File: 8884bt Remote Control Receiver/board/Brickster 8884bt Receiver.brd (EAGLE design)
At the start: 28.8 x 28.8 mm, 22 parts, among them IC2 IC_RT9164A, J1 AVR_SPI_PRG_6NS, J2 CON_PF, J3 CON_PF, J4 CON_PF, U1 IC_ATTINY_X4A, U2 IC_TB6612FNG

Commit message: Add second mounting tab
provides more stability
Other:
- outline, holes or cut-outs redrawn
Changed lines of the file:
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@@
 <wire x1="0" y1="19.9644" x2="0.8128" y2="20.7772" width="0" layer="20" curve="-90"/>
 <wire x1="28.7528" y1="19.9644" x2="27.94" y2="20.7772" width="0" layer="20" curve="90"/>
-<wire x1="10.3886" y1="21.1836" x2="10.3886" y2="27.94" width="0" layer="20"/>
-<wire x1="9.5758" y1="28.7528" x2="7.2644" y2="28.7528" width="0" layer="20"/>
-<wire x1="5.588" y1="28.7528" x2="3.2258" y2="28.7528" width="0" layer="20"/>
-<wire x1="2.413" y1="27.94" x2="2.413" y2="21.1836" width="0" layer="20"/>
-<wire x1="4.064" y1="26.3398" x2="8.7376" y2="26.3398" width="0" layer="20" curve="180"/>
-<wire x1="4.064" y1="26.3398" x2="5.588" y2="28.5496" width="0" layer="20" curve="-69.007147"/>
-<wire x1="8.7376" y1="26.3398" x2="7.2644" y2="28.5496" width="0" layer="20" curve="69.007147"/>
-<wire x1="2.0066" y1="20.7772" x2="2.413" y2="21.1836" width="0" layer="20" curve="90"/>
-<wire x1="10.3886" y1="21.1836" x2="10.795" y2="20.7772" width="0" layer="20" curve="90"/>
-<wire x1="2.413" y1="27.94" x2="3.2258" y2="28.7528" width="0" layer="20" curve="-90"/>
-<wire x1="9.5758" y1="28.7528" x2="10.3886" y2="27.94" width="0" layer="20" curve="-90"/>
-<wire x1="5.588" y1="28.7528" x2="5.588" y2="28.5496" width="0" layer="20" curve="-180"/>
-<wire x1="7.2644" y1="28.7528" x2="7.2644" y2="28.5496" width="0" layer="20" curve="180"/>
-<wire x1="26.3398" y1="21.1836" x2="26.3398" y2="27.94" width="0" layer="20"/>
-<wire x1="25.527" y1="28.7528" x2="23.2156" y2="28.7528" width="0" layer="20"/>
-<wire x1="21.5392" y1="28.7528" x2="19.177" y2="28.7528" width="0" layer="20"/>
-<wire x1="18.3642" y1="27.94" x2="18.3642" y2="21.1836" width="0" layer="20"/>
-<wire x1="20.0152" y1="26.3398" x2="24.6888" y2="26.3398" width="0" layer="20" curve="180"/>
-<wire x1="20.0152" y1="26.3398" x2="21.5392" y2="28.5496" width="0" layer="20" curve="-69.007147"/>
-<wire x1="24.6888" y1="26.3398" x2="23.2156" y2="28.5496" width="0" layer="20" curve="69.007147"/>
-<wire x1="17.9578" y1="20.7772" x2="18.3642" y2="21.1836" width="0" layer="20" curve="90"/>
-<wire x1="26.3398" y1="21.1836" x2="26.7462" y2="20.7772" width="0" layer="20" curve="90"/>
-<wire x1="18.3642" y1="27.94" x2="19.177" y2="28.7528" width="0" layer="20" curve="-90"/>
-<wire x1="25.527" y1="28.7528" x2="26.3398" y2="27.94" width="0" layer="20" curve="-90"/>
-<wire x1="21.5392" y1="28.7528" x2="21.5392" y2="28.5496" width="0" layer="20" curve="-180"/>
-<wire x1="23.2156" y1="28.7528" x2="23.2156" y2="28.5496" width="0" layer="20" curve="180"/>
-<wire x1="10.795" y1="20.7772" x2="17.9578" y2="20.7772" width="0" layer="20"/>
-<wire x1="0.8128" y1="20.7772" x2="2.0066" y2="20.7772" width="0" layer="20"/>
-<wire x1="27.94" y1="20.7772" x2="26.7462" y2="20.7772" width="0" layer="20"/>
-<dimension x1="0" y1="20.7772" x2="3.2258" y2="28.7528" x3="-1.3462" y3="24.765" textsize="1.778" layer="49" dtype="vertical" width="0.1"/>
-<dimension x1="2.413" y1="27.94" x2="10.3886" y2="27.94" x3="6.4008" y3="29.5148" textsize="1.778" layer="49" dtype="horizontal" width="0.1"/>
-<dimension x1="10.3886" y1="27.94" x2="18.3642" y2="27.94" x3="14.3764" y3="29.5148" textsize="1.778" layer="49" dtype="horizontal" width="0.1"/>
-<dimension x1="18.3642" y1="27.94" x2="26.3398" y2="27.94" x3="22.352" y3="29.4894" textsize="1.778" layer="49" dtype="horizontal" width="0.1"/>
-<dimension x1="4.064" y1="26.3398" x2="8.7376" y2="26.3398" x3="6.4008" y3="24.6888" textsize="1.778" layer="49" dtype="horizontal" width="0.1"/>
+<wire x1="10.3759" y1="20.7772" x2="10.3759" y2="27.9654" width="0" layer="20"/>
+<wire x1="9.5631" y1="28.7782" x2="3.1877" y2="28.7782" width="0" layer="20"/>
+<wire x1="2.3749" y1="27.9654" x2="2.3749" y2="20.7772" width="0" layer="20"/>
+<wire x1="2.3749" y1="27.9654" x2="3.1877" y2="28.7782" width="0" layer="20" curve="-90"/>
+<wire x1="9.5631" y1="28.7782" x2="10.3759" y2="27.9654" width="0" layer="20" curve="-90"/>
+<wire x1="26.3779" y1="20.7772" x2="26.3779" y2="27.9654" width="0" layer="20"/>
+<wire x1="25.5651" y1="28.7782" x2="19.1897" y2="28.7782" width="0" layer="20"/>
+<wire x1="18.3769" y1="27.9654" x2="18.3769" y2="20.7772" width="0" layer="20"/>
+<wire x1="18.3769" y1="27.9654" x2="19.1897" y2="28.7782" width="0" layer="20" curve="-90"/>
+<wire x1="25.5651" y1="28.7782" x2="26.3779" y2="27.9654" width="0" layer="20" curve="-90"/>
+<wire x1="10.3759" y1="20.7772" x2="18.3769" y2="20.7772" width="0" layer="20"/>
+<wire x1="0.8128" y1="20.7772" x2="2.3749" y2="20.7772" width="0" layer="20"/>
+<wire x1="27.94" y1="20.7772" x2="26.3779" y2="20.7772" width="0" layer="20"/>
+<dimension x1="0" y1="20.7772" x2="3.2004" y2="28.7782" x3="-1.3462" y3="24.7777" textsize="1.778" layer="49" dtype="vertical" width="0.1"/>
+<dimension x1="2.3749" y1="27.9654" x2="10.3759" y2="27.9654" x3="6.3754" y3="29.5148" textsize="1.778" layer="49" dtype="horizontal" width="0.1"/>
+<dimension x1="10.3759" y1="27.9654" x2="18.3769" y2="27.9654" x3="14.3764" y3="29.5148" textsize="1.778" layer="49" dtype="horizontal" width="0.1"/>
+<dimension x1="18.3769" y1="27.9654" x2="26.3779" y2="27.9654" x3="22.3774" y3="29.4894" textsize="1.778" layer="49" dtype="horizontal" width="0.1"/>
+<hole x="6.3754" y="24.7777" drill="4.75"/>
+<hole x="22.3774" y="24.7777" drill="4.75"/>
+<dimension x1="8.7504" y1="24.7777" x2="4.0004" y2="24.765" x3="4.0004" y3="24.765" textsize="1.778" layer="49" dtype="diameter" width="0.1"/>
 </plain>
 <attributes>

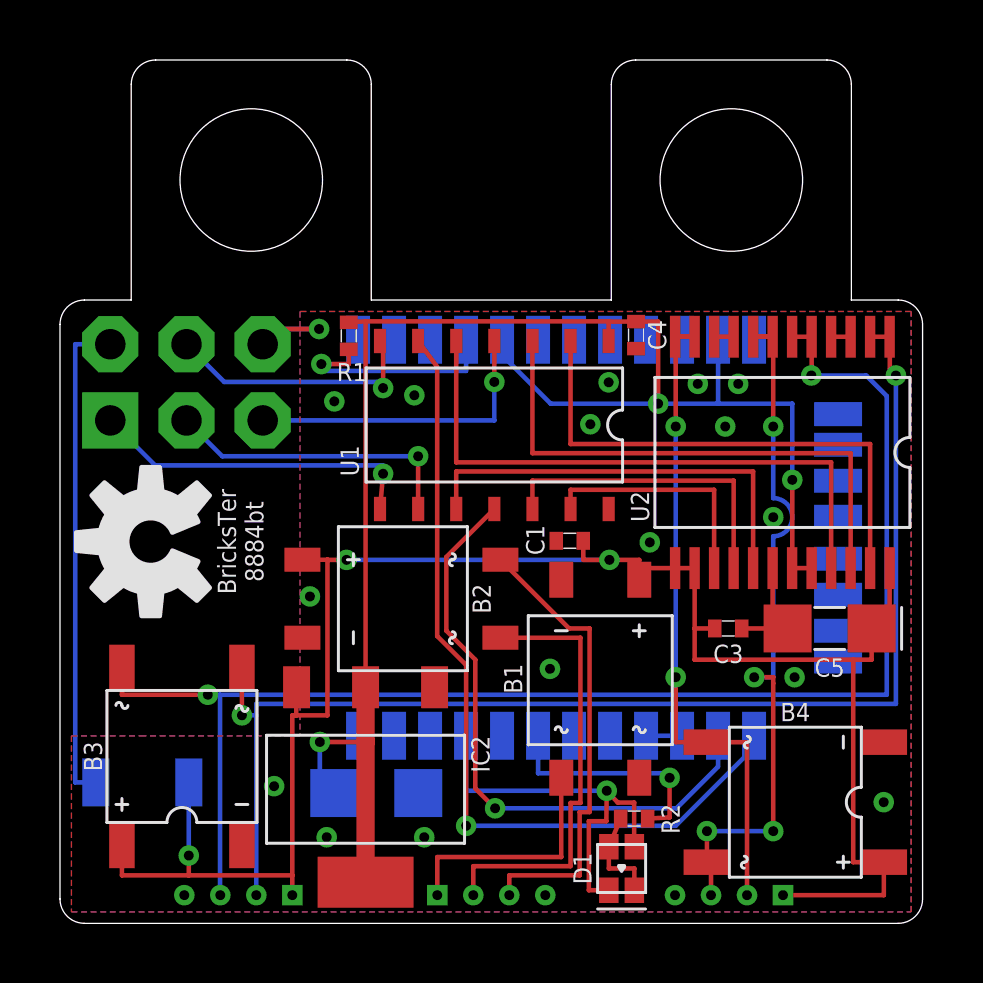
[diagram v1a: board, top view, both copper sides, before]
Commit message: Widen PF drills
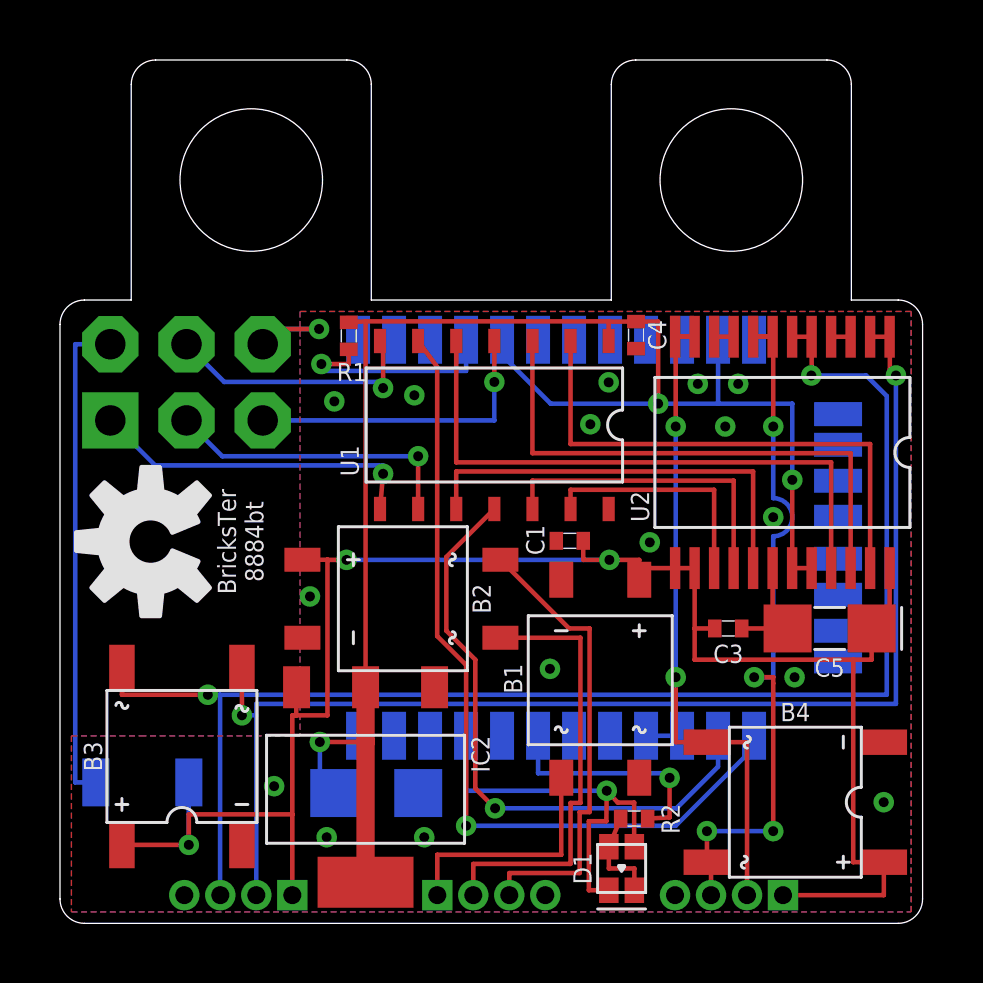
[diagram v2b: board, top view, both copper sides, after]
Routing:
- net VIN: track 64.2 -> 63.2 mm
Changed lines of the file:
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@@
 <hole x="6.3754" y="24.7777" drill="4.75"/>
 <hole x="22.3774" y="24.7777" drill="4.75"/>
-<dimension x1="8.7504" y1="24.7777" x2="4.0004" y2="24.765" x3="4.0004" y3="24.765" textsize="1.778" layer="49" dtype="diameter" width="0.1"/>
+<dimension x1="8.7504" y1="24.7777" x2="4.0004" y2="24.7777" x3="4.0004" y3="24.7777" textsize="1.778" layer="49" dtype="diameter" width="0.1"/>
 </plain>
 <attributes>
@@
 <contactref element="J3" pad="9V"/>
 <contactref element="J4" pad="9V"/>
-<wire x1="2.064" y1="2.6126" x2="2.064" y2="1.6002" width="0.1524" layer="1"/>
-<wire x1="2.064" y1="1.6002" x2="4.2926" y2="1.6002" width="0.1524" layer="1"/>
-<wire x1="4.2926" y1="1.6002" x2="7.7436" y2="1.6002" width="0.1524" layer="1"/>
-<wire x1="7.7436" y1="1.6002" x2="7.7436" y2="0.9398" width="0.1524" layer="1"/>
 <wire x1="8.0792" y1="12.1204" x2="8.9154" y2="12.1204" width="0.1524" layer="1"/>
 <wire x1="8.9154" y1="12.1158" x2="8.9154" y2="6.9342" width="0.1524" layer="1"/>
 <wire x1="8.9154" y1="6.9342" x2="7.874" y2="6.9342" width="0.1524" layer="1"/>
 <wire x1="7.874" y1="6.9342" x2="7.7436" y2="6.9342" width="0.1524" layer="1"/>
-<wire x1="7.7436" y1="6.9342" x2="7.7436" y2="1.6002" width="0.1524" layer="1"/>
+<wire x1="7.7436" y1="6.9342" x2="7.7436" y2="3.6322" width="0.1524" layer="1"/>
+<wire x1="7.7436" y1="3.6322" x2="7.7436" y2="0.9398" width="0.1524" layer="1"/>
 <wire x1="7.8854" y1="7.8704" x2="7.874" y2="6.9342" width="0.1524" layer="1"/>
 <wire x1="24.1012" y1="0.9398" x2="27.461" y2="0.9398" width="0.1524" layer="1"/>
@@
 <wire x1="17.4426" y1="12.7508" x2="17.4426" y2="12.1158" width="0.1524" layer="1"/>
 <wire x1="17.4426" y1="12.1158" x2="18.3134" y2="12.1158" width="0.1524" layer="1"/>
-<via x="4.2926" y="2.2606" extent="1-16" drill="0.3302"/>
-<wire x1="4.2926" y1="2.2606" x2="4.2926" y2="1.6002" width="0.1524" layer="1"/>
+<via x="4.2926" y="2.6162" extent="1-16" drill="0.3302"/>
 <contactref element="D2" pad="2"/>
 <contactref element="U2" pad="13"/>
@@
 <wire x1="20.5042" y1="11.8412" x2="19.3086" y2="11.8412" width="0.1524" layer="1"/>
 <wire x1="19.3086" y1="11.8412" x2="19.3086" y2="11.4534" width="0.1524" layer="1"/>
-<wire x1="4.2932" y1="4.699" x2="4.2926" y2="2.2606" width="0.1524" layer="16"/>
+<wire x1="4.2932" y1="4.699" x2="4.2926" y2="2.6162" width="0.1524" layer="16"/>
 <wire x1="27.054" y1="8.7884" x2="27.054" y2="9.8298" width="0.1524" layer="1"/>
+<wire x1="2.064" y1="2.6126" x2="2.064" y2="2.6162" width="0.1524" layer="1"/>
+<wire x1="2.064" y1="2.6162" x2="4.2926" y2="2.6162" width="0.1524" layer="1"/>
+<wire x1="4.2926" y1="2.6162" x2="4.2926" y2="3.6322" width="0.1524" layer="1"/>
+<wire x1="4.2926" y1="3.6322" x2="7.7436" y2="3.6322" width="0.1524" layer="1"/>
 </signal>
 <signal name="BLUE">
@@
 <contactref element="B1" pad="AC1"/>
 <contactref element="J2" pad="9V"/>
-<wire x1="12.5764" y1="0.9398" x2="12.5764" y2="2.2098" width="0.1524" layer="1"/>
-<wire x1="12.5764" y1="2.2098" x2="16.7086" y2="2.2098" width="0.1524" layer="1"/>
-<wire x1="16.7086" y1="2.2098" x2="16.7086" y2="4.8534" width="0.1524" layer="1"/>
+<wire x1="12.5764" y1="0.9398" x2="12.5764" y2="2.286" width="0.1524" layer="1"/>
+<wire x1="12.5764" y1="2.286" x2="16.7086" y2="2.286" width="0.1524" layer="1"/>
+<wire x1="16.7086" y1="2.286" x2="16.7086" y2="4.8534" width="0.1524" layer="1"/>
 </signal>
 <signal name="PF_C1">
 <contactref element="J2" pad="C1"/>
 <contactref element="B2" pad="AC2"/>
-<wire x1="14.9764" y1="0.9398" x2="14.9764" y2="1.6002" width="0.1524" layer="1"/>
-<wire x1="14.9764" y1="1.6002" x2="17.3228" y2="1.6002" width="0.1524" layer="1"/>
-<wire x1="17.3228" y1="1.6002" x2="17.3228" y2="3.7084" width="0.1524" layer="1"/>
+<wire x1="14.9764" y1="0.9398" x2="14.9764" y2="1.6764" width="0.1524" layer="1"/>
+<wire x1="14.9764" y1="1.6764" x2="17.3228" y2="1.6764" width="0.1524" layer="1"/>
+<wire x1="17.3228" y1="1.6764" x2="17.3228" y2="3.7084" width="0.1524" layer="1"/>
 <wire x1="17.3228" y1="3.7084" x2="17.653" y2="3.7084" width="0.1524" layer="1"/>
 <wire x1="17.653" y1="3.7084" x2="17.653" y2="9.8298" width="0.1524" layer="1"/>
@@
 <contactref element="J2" pad="C2"/>
 <contactref element="B2" pad="AC1"/>
-<wire x1="13.7764" y1="0.9398" x2="13.7764" y2="1.905" width="0.1524" layer="1"/>
-<wire x1="13.7764" y1="1.905" x2="17.018" y2="1.905" width="0.1524" layer="1"/>
-<wire x1="17.018" y1="1.905" x2="17.018" y2="4.0132" width="0.1524" layer="1"/>
+<wire x1="13.7764" y1="0.9398" x2="13.7764" y2="1.9812" width="0.1524" layer="1"/>
+<wire x1="13.7764" y1="1.9812" x2="17.018" y2="1.9812" width="0.1524" layer="1"/>
+<wire x1="17.018" y1="1.9812" x2="17.018" y2="4.0132" width="0.1524" layer="1"/>
 <wire x1="17.018" y1="4.0132" x2="17.3482" y2="4.0132" width="0.1524" layer="1"/>
 <wire x1="17.3482" y1="4.0132" x2="17.3482" y2="9.5204" width="0.1524" layer="1"/>
